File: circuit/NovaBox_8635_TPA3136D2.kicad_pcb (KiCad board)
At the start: 2 copper layers, 100 x 82 mm, 80 parts, among them J1 CONN_01X11, J10 CONN_01X02, J11 CONN_01X03, J12 CONN_01X02, J13 CONN_01X02, J14 CONN_01X04, J2 CONN_01X15, J3 CONN_01X02, J5 CONN_01X02, J6 USB_B, J7 CONN_01X04, J8 CONN_01X04, J9 CONN_01X02, Q1 IRLML6401, Q2 IRLML6401, Q3 MMBT3904, Q4 MMBT3904, SW1 PIO8, SW2 PIO6, SW3 SPI_PCM, SW4 CSR_RST, SW5 MFB_SW, U1 CSR8635_MODULE, U2 CSR_DebugSmall, U3 TPA3136D2

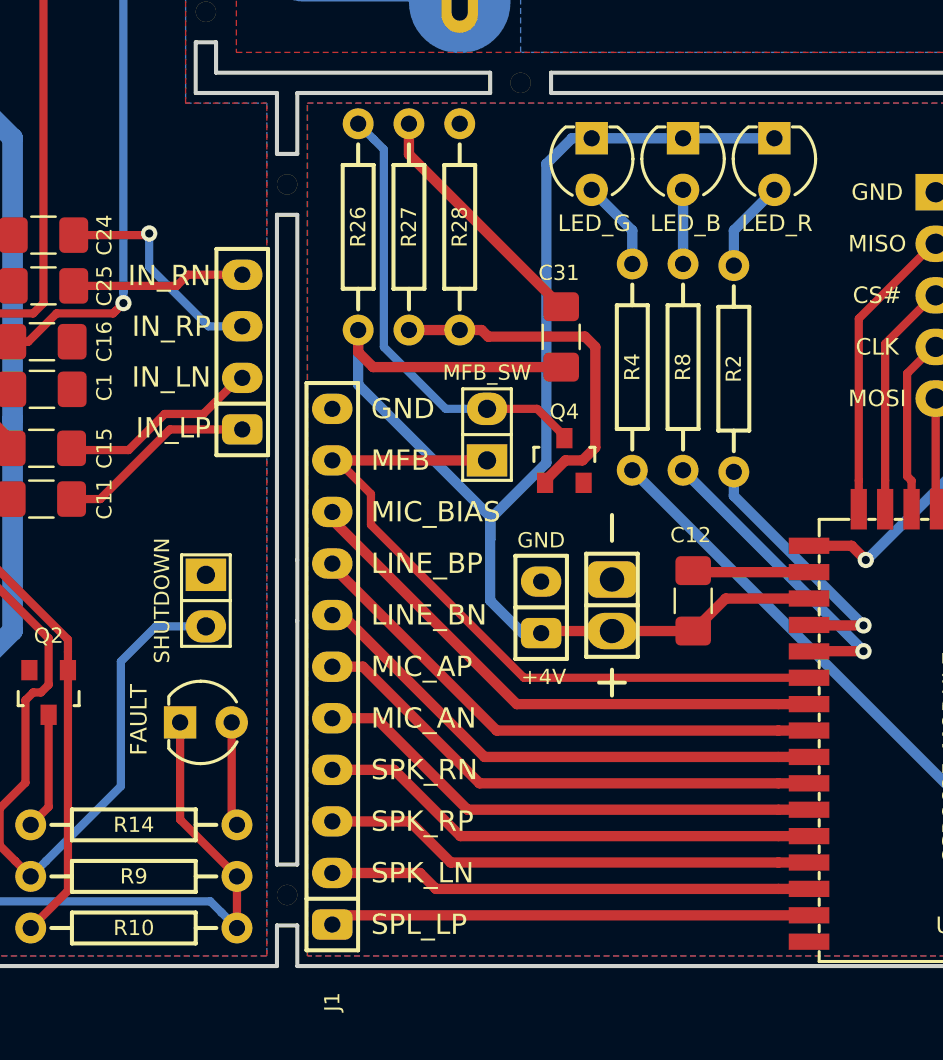
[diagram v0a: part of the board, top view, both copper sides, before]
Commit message: started Power; still need to change transistor on TPA3136; lengthen the pads on HTSSOP
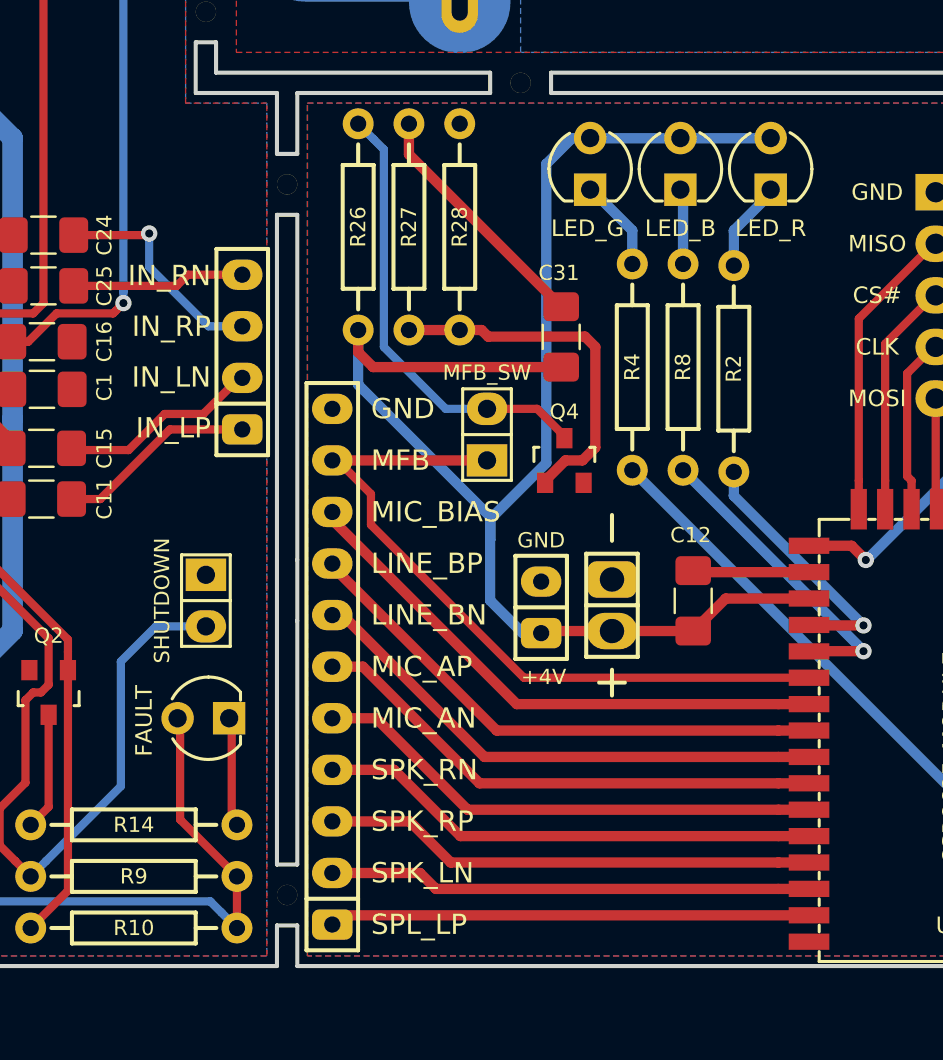
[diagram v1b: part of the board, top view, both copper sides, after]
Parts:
- moved D3 0.24 mm to (79.4, 137.8), turned to 0 degrees
- moved D1 0.19 mm to (107.3, 110.5), turned to 270 degrees
- moved D4 0.13 mm to (102.9, 110.5), turned to 270 degrees
- moved D2 0.08 mm to (98.4, 110.5), turned to 270 degrees
